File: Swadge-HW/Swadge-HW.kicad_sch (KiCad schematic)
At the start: 90 parts, among them J1 SAO, J2 PJ-307C, J3 PGM, P1 USB_C_Plug_USB2.0, Q1 Q_PMOS_GSD, SW1 YTS-D003-1A, SW2 YTS-D003-1A, SW3 YTS-D003-1A, SW4 YTS-D003-1A, SW5 YTS-D003-1A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

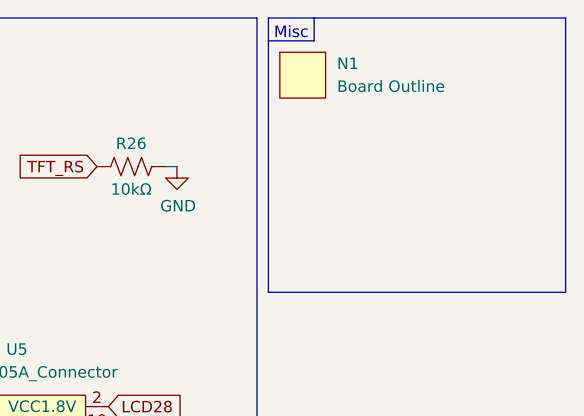
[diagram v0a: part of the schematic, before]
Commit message: Added condiment part
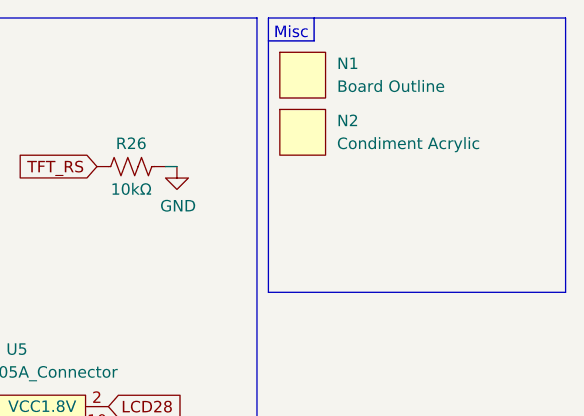
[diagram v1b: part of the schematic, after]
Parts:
- added N2: Condiment Acrylic, Swadge_Hotdog:condiment, symbol Swadge_Parts:NULL
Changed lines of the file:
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@@
+	)
+	(symbol
+		(lib_id "Swadge_Parts:NULL")
+		(at 313.69 25.4 0)
+		(unit 1)
+		(exclude_from_sim no)
+		(in_bom yes)
+		(on_board yes)
+		(dnp no)
+		(fields_autoplaced yes)
+		(property "Reference" "N2"
+			(at 317.5 24.1299 0)
+			(effects
+				(font
+					(size 1.27 1.27)
+				)
+				(justify left)
+			)
+		)
+		(property "Value" "Condiment Acrylic"
+			(at 317.5 26.6699 0)
+			(effects
+				(font
+					(size 1.27 1.27)
+				)
+				(justify left)
+			)
+		)
+		(property "Footprint" "Swadge_Hotdog:condiment"
+			(at 313.69 25.4 0)
+			(effects
+				(font
+					(size 1.27 1.27)
+				)
+				(hide yes)
+			)
+		)
+		(property "Datasheet" ""
+			(at 313.69 25.4 0)
+			(effects
+				(font
+					(size 1.27 1.27)
+				)
+				(hide yes)
+			)
+		)
+		(property "Description" ""
+			(at 313.69 25.4 0)
+			(effects
+				(font
+					(size 1.27 1.27)
+				)
+				(hide yes)
+			)
+		)
+		(instances
+			(project ""
+				(path "/770c762f-3a30-4864-b7da-de353459cdd6"
+					(reference "N2")
+					(unit 1)
+				)
+			)
+		)
 	)
 	(symbol

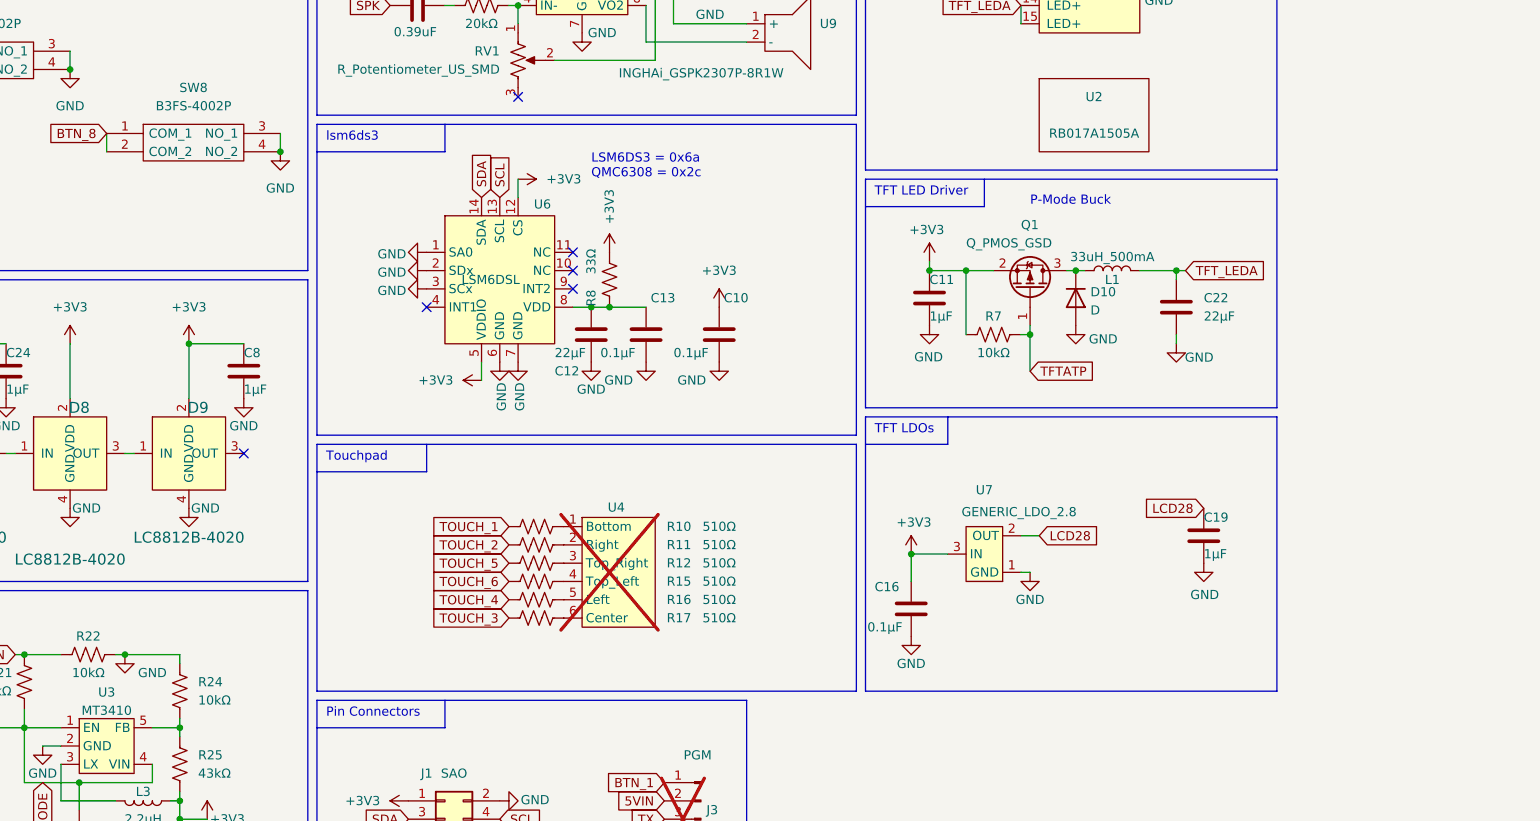
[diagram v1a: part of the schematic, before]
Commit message: Layout v0.5
Placement of 80% of SMD components
Add QMC6309
DNP D9
Move Power Switch to right dog
Bump Aux port over
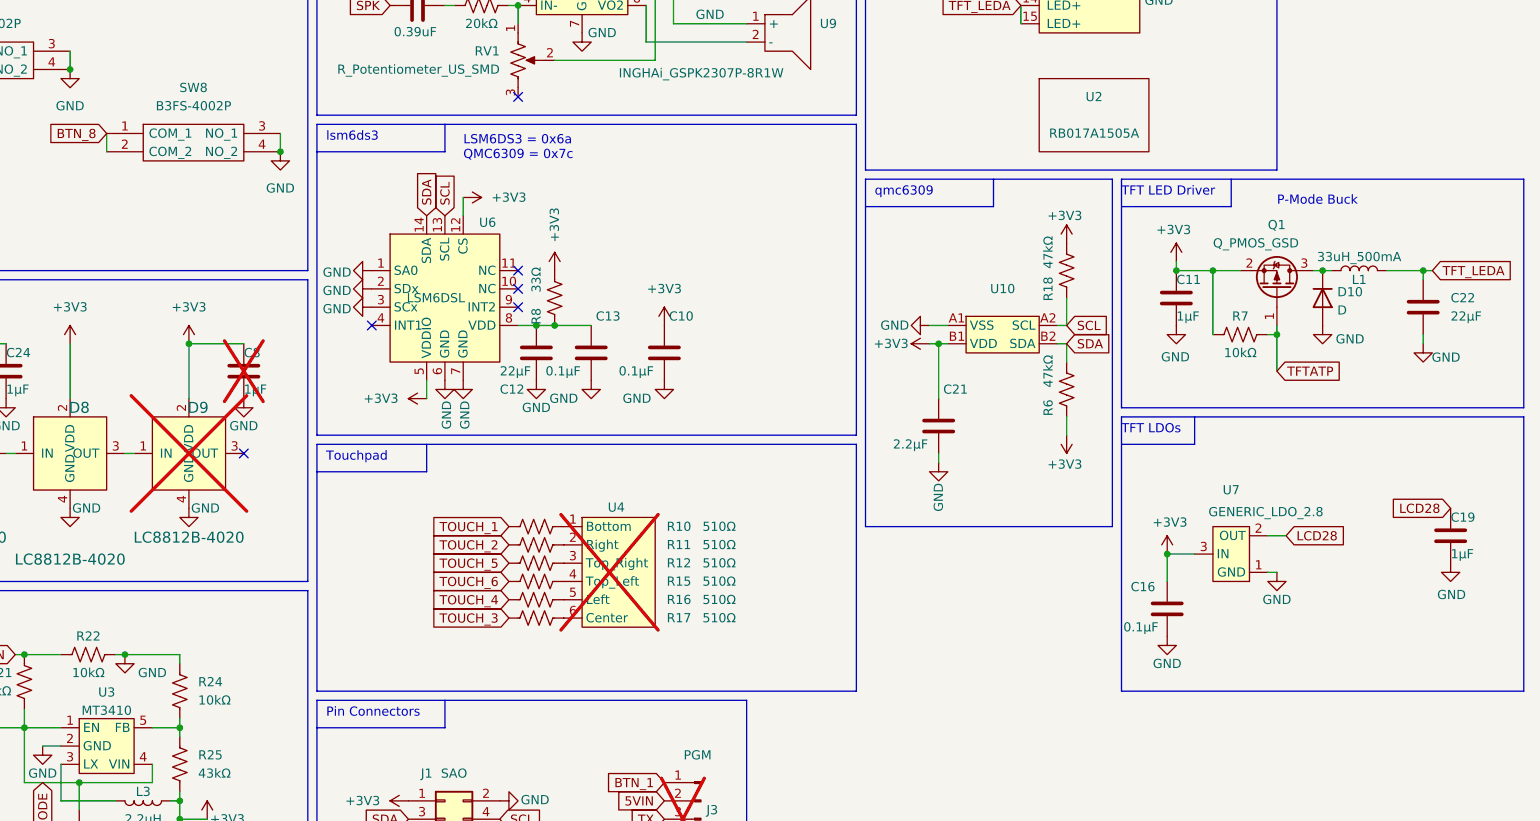
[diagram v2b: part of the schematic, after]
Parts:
- added C21: 2.2μF, Swadge_Parts:C_0603_1608Metric, symbol Swadge_Parts:C
- added R18, R6: 47kΩ, Swadge_Parts:R_0603_1608Metric, symbol Swadge_Parts:R_US
- added U10: ~, Swadge_Parts:BGA-4-.83x.83, symbol Swadge_Parts:QMC6309
- C8, D9: now not fitted
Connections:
- net +3V3: now also C21.1, R18.2, R6.1, U10.B1 (VDD)
- net GND: now also C21.2, U10.A1 (VSS)
- net SCL: now also R18.1, U10.A2 (SCL)
- net SDA: now also R6.2, U10.B2 (SDA)
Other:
- note added: "LSM6DS3 = 0x6a QMC6309 = 0x7c"
- note added: "qmc6309"
- note removed: "LSM6DS3 = 0x6a QMC6308 = 0x2c"
- moved on the sheet: C10, C11, C12, C13, C16, C19, C22, D10, L1, Q1, R7, R8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

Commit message: update from changes made by charlesl pre-order
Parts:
- N1: now not fitted
- N2: now not fitted; now left out of the parts list
- R18, R6: value 47kΩ -> 10kΩ; Cost @ 2.5k 0.0008 -> 0.0007; LCSC C23140 -> C25804
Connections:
- net +3V3: now also R18.1, R6.2; no longer R18.2, R6.1
- net SCL: now also R6.1; no longer R18.1
- net SDA: now also R18.2; no longer R6.2
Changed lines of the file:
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@@
 	)
 	(symbol
+		(lib_id "Swadge_Parts:R_US")
+		(at 279.4 113.03 180)
+		(unit 1)
+		(exclude_from_sim no)
+		(in_bom yes)
+		(on_board yes)
+		(dnp no)
+		(property "Reference" "R6"
+			(at 276.86 113.03 90)
+			(effects
+				(font
+					(size 1.27 1.27)
+				)
+			)
+		)
+		(property "Value" "10kΩ"
+			(at 281.94 113.03 90)
+			(effects
+				(font
+					(size 1.27 1.27)
+				)
+			)
+		)
+		(property "Footprint" "Swadge_Parts:R_0603_1608Metric"
+			(at 278.384 112.776 90)
+			(effects
+				(font
+					(size 1.27 1.27)
+				)
+				(hide yes)
+			)
+		)
+		(property "Datasheet" "~"
+			(at 276.86 113.03 90)
+			(effects
+				(font
+					(size 1.27 1.27)
+				)
+				(hide yes)
+			)
+		)
+		(property "Description" ""
+			(at 279.4 113.03 0)
+			(effects
+				(font
+					(size 1.27 1.27)
+				)
+				(hide yes)
+			)
+		)
+		(property "Digikey" "~"
+			(at 274.32 115.57 90)
+			(effects
+				(font
+					(size 1.27 1.27)
+				)
+				(hide yes)
+			)
+		)
+		(property "Cost100" "10"
+			(at 279.4 113.03 0)
+			(effects
+				(font
+					(size 0.254 0.254)
+				)
+				(hide yes)
+			)
+		)
+		(property "Substitutable" "Y"
+			(at 279.4 113.03 0)
+			(effects
+				(font
+					(size 0.254 0.254)
+				)
+				(hide yes)
+			)
+		)
+		(property "LCSC" "C25804"
+			(at 279.4 113.03 0)
+			(effects
+				(font
+					(size 1.27 1.27)
+				)
+				(hide yes)
+			)
+		)
+		(property "Cost @ 2.5k" "0.0007"
+			(at 279.4 113.03 0)
+			(effects
+				(font
+					(size 1.27 1.27)
+				)
+				(hide yes)
+			)
+		)
+		(pin "1"
+		)
+		(pin "2"
+		)
+		(instances
+			(project "Swadge-HW"
+				(path "/770c762f-3a30-4864-b7da-de353459cdd6"
+					(reference "R6")
+					(unit 1)
+				)
+			)
+		)
+	)
+	(symbol
 		(lib_id "Swadge_Parts:GND")
 		(at 332.74 153.67 0)
@@
 	)
 	(symbol
-		(lib_id "Swadge_Parts:R_US")
-		(at 279.4 113.03 180)
-		(unit 1)
-		(exclude_from_sim no)
-		(in_bom yes)
-		(on_board yes)
-		(dnp no)
-		(property "Reference" "R18"
-			(at 276.86 115.57 90)
-			(effects
-				(font
-					(size 1.27 1.27)
-				)
-			)
-		)
-		(property "Value" "47kΩ"
-			(at 276.86 110.49 90)
-			(effects
-				(font
-					(size 1.27 1.27)
-				)
-			)
-		)
-		(property "Footprint" "Swadge_Parts:R_0603_1608Metric"
-			(at 278.384 112.776 90)
-			(effects
-				(font
-					(size 1.27 1.27)
-				)
-				(hide yes)
-			)
-		)
-		(property "Datasheet" "~"
-			(at 279.4 113.03 0)
-			(effects
-				(font
-					(size 1.27 1.27)
-				)
-				(hide yes)
-			)
-		)
-		(property "Description" ""
-			(at 279.4 113.03 0)
-			(effects
-				(font
-					(size 1.27 1.27)
-				)
-				(hide yes)
-			)
-		)
-		(property "Cost100" "10"
-			(at 322.58 -12.7 0)
-			(effects
-				(font
-					(size 1.27 1.27)
-				)
-				(hide yes)
-			)
-		)
-		(property "Digikey" "~"
-			(at 322.58 -12.7 0)
-			(effects
-				(font
-					(size 1.27 1.27)
-				)
-				(hide yes)
-			)
-		)
-		(property "Substitutable" "Y"
-			(at 322.58 -12.7 0)
-			(effects
-				(font
-					(size 1.27 1.27)
-				)
-				(hide yes)
-			)
-		)
-		(property "LCSC" "C23140"
-			(at 279.4 113.03 0)
-			(effects
-				(font
-					(size 1.27 1.27)
-				)
-				(hide yes)
-			)
-		)
-		(property "Cost @ 2.5k" "0.0008"
-			(at 279.4 113.03 0)
-			(effects
-				(font
-					(size 1.27 1.27)
-				)
-				(hide yes)
-			)
-		)
-		(pin "1"
-		)
-		(pin "2"
-		)
-		(instances
-			(project "Swadge-HW"
-				(path "/770c762f-3a30-4864-b7da-de353459cdd6"
-					(reference "R18")
-					(unit 1)
-				)
-			)
-		)
-	)
-	(symbol
 		(lib_id "Swadge_Parts:YTS-D003-1A")
 		(at 129.54 63.5 0)
@@
 	)
 	(symbol
+		(lib_id "Swadge_Parts:R_US")
+		(at 279.4 129.54 180)
+		(unit 1)
+		(exclude_from_sim no)
+		(in_bom yes)
+		(on_board yes)
+		(dnp no)
+		(property "Reference" "R18"
+			(at 276.86 129.54 90)
+			(effects
+				(font
+					(size 1.27 1.27)
+				)
+			)
+		)
+		(property "Value" "10kΩ"
+			(at 281.94 129.54 90)
+			(effects
+				(font
+					(size 1.27 1.27)
+				)
+			)
+		)
+		(property "Footprint" "Swadge_Parts:R_0603_1608Metric"
+			(at 278.384 129.286 90)
+			(effects
+				(font
+					(size 1.27 1.27)
+				)
+				(hide yes)
+			)
+		)
+		(property "Datasheet" "~"
+			(at 276.86 129.54 90)
+			(effects
+				(font
+					(size 1.27 1.27)
+				)
+				(hide yes)
+			)
+		)
+		(property "Description" ""
+			(at 279.4 129.54 0)
+			(effects
+				(font
+					(size 1.27 1.27)
+				)
+				(hide yes)
+			)
+		)
+		(property "Digikey" "~"
+			(at 274.32 132.08 90)
+			(effects
+				(font
+					(size 1.27 1.27)
+				)
+				(hide yes)
+			)
+		)
+		(property "Cost100" "10"
+			(at 279.4 129.54 0)
+			(effects
+				(font
+					(size 0.254 0.254)
+				)
+				(hide yes)
+			)
+		)
+		(property "Substitutable" "Y"
+			(at 279.4 129.54 0)
+			(effects
+				(font
+					(size 0.254 0.254)
+				)
+				(hide yes)
+			)
+		)
+		(property "LCSC" "C25804"
+			(at 279.4 129.54 0)
+			(effects
+				(font
+					(size 1.27 1.27)
+				)
+				(hide yes)
+			)
+		)
+		(property "Cost @ 2.5k" "0.0007"
+			(at 279.4 129.54 0)
+			(effects
+				(font
+					(size 1.27 1.27)
+				)
+				(hide yes)
+			)
+		)
+		(pin "1"
+		)
+		(pin "2"
+		)
+		(instances
+			(project "Swadge-HW"
+				(path "/770c762f-3a30-4864-b7da-de353459cdd6"
+					(reference "R18")
+					(unit 1)
+				)
+			)
+		)
+	)
+	(symbol
 		(lib_id "Swadge_Parts:GND")
 		(at 294.64 120.65 0)
@@
 	)
 	(symbol
-		(lib_id "Swadge_Parts:R_US")
-		(at 279.4 129.54 180)
-		(unit 1)
-		(exclude_from_sim no)
-		(in_bom yes)
-		(on_board yes)
-		(dnp no)
-		(property "Reference" "R6"
-			(at 276.86 132.08 90)
-			(effects
-				(font
-					(size 1.27 1.27)
-				)
-			)
-		)
-		(property "Value" "47kΩ"
-			(at 276.86 127 90)
-			(effects
-				(font
-					(size 1.27 1.27)
-				)
-			)
-		)
-		(property "Footprint" "Swadge_Parts:R_0603_1608Metric"
-			(at 278.384 129.286 90)
-			(effects
-				(font
-					(size 1.27 1.27)
-				)
-				(hide yes)
-			)
-		)
-		(property "Datasheet" "~"
-			(at 279.4 129.54 0)
-			(effects
-				(font
-					(size 1.27 1.27)
-				)
-				(hide yes)
-			)
-		)
-		(property "Description" ""
-			(at 279.4 129.54 0)
-			(effects
-				(font
-					(size 1.27 1.27)
-				)
-				(hide yes)
-			)
-		)
-		(property "Cost100" "10"
-			(at 322.58 3.81 0)
-			(effects
-				(font
-					(size 1.27 1.27)
-				)
-				(hide yes)
-			)
-		)
-		(property "Digikey" "~"
-			(at 322.58 3.81 0)
-			(effects
-				(font
-					(size 1.27 1.27)
-				)
-				(hide yes)
-			)
-		)
-		(property "Substitutable" "Y"
-			(at 322.58 3.81 0)
-			(effects
-				(font
-					(size 1.27 1.27)
-				)
-				(hide yes)
-			)
-		)
-		(property "LCSC" "C23140"
-			(at 279.4 129.54 0)
-			(effects
-				(font
-					(size 1.27 1.27)
-				)
-				(hide yes)
-			)
-		)
-		(property "Cost @ 2.5k" "0.0008"
-			(at 279.4 129.54 0)
-			(effects
-				(font
-					(size 1.27 1.27)
-				)
-				(hide yes)
-			)
-		)
-		(pin "1"
-		)
-		(pin "2"
-		)
-		(instances
-			(project "Swadge-HW"
-				(path "/770c762f-3a30-4864-b7da-de353459cdd6"
-					(reference "R6")
-					(unit 1)
-				)
-			)
-		)
-	)
-	(symbol
 		(lib_id "Swadge_Parts:+3.3V")
 		(at 294.64 111.76 0)
@@
 		(unit 1)
 		(exclude_from_sim no)
-		(in_bom yes)
+		(in_bom no)
 		(on_board yes)
-		(dnp no)
+		(dnp yes)
 		(fields_autoplaced yes)
 		(property "Reference" "N2"
@@
 		(in_bom no)
 		(on_board yes)
-		(dnp no)
+		(dnp yes)
 		(fields_autoplaced yes)
 		(property "Reference" "N1"

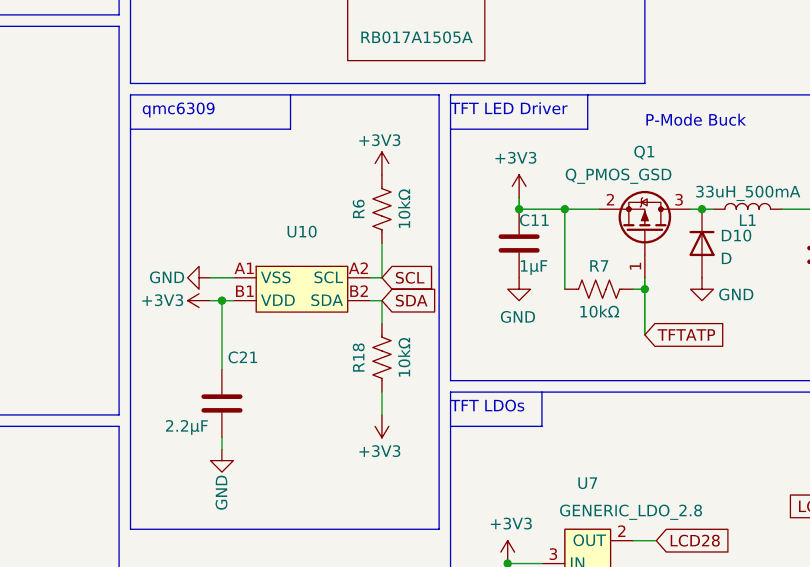
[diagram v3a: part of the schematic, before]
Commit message: Update to order for rev - before checking footprint on ESP32-S2
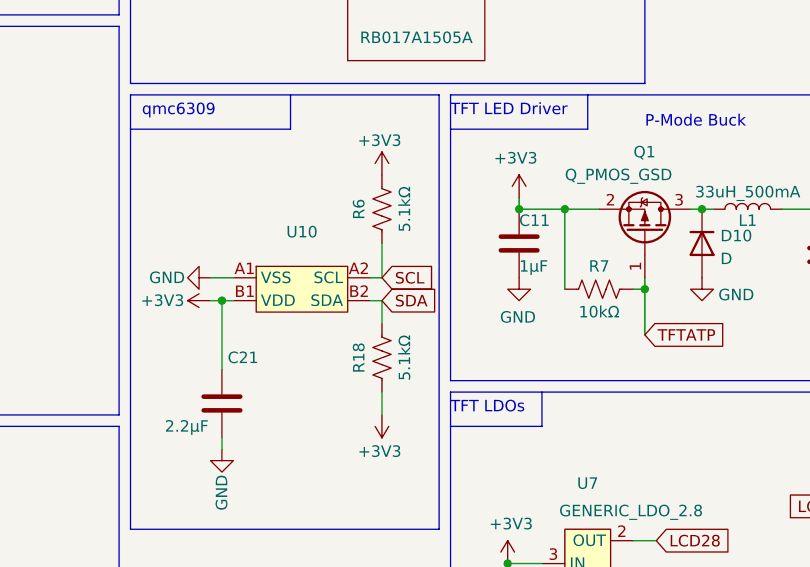
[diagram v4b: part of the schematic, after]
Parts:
- R18, R6: value 10kΩ -> 5.1kΩ; LCSC C25804 -> C23186
- RV1: LCSC C470765 -> C3020613
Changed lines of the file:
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@@
 			)
 		)
-		(property "Description" "RK10J11R001Y"
+		(property "Description" "RK10J11R0A0L"
 			(at 203.2 83.82 0)
 			(effects
@@
 			)
 		)
-		(property "LCSC" "C470765"
+		(property "LCSC" "C3020613"
 			(at 203.2 101.6 0)
 			(effects
@@
 			)
 		)
-		(property "Value" "10kΩ"
+		(property "Value" "5.1kΩ"
 			(at 281.94 113.03 90)
 			(effects
@@
 			)
 		)
-		(property "LCSC" "C25804"
+		(property "LCSC" "C23186"
 			(at 279.4 113.03 0)
 			(effects
@@
 			)
 		)
-		(property "Value" "10kΩ"
+		(property "Value" "5.1kΩ"
 			(at 281.94 129.54 90)
 			(effects
@@
 			)
 		)
-		(property "LCSC" "C25804"
+		(property "LCSC" "C23186"
 			(at 279.4 129.54 0)
 			(effects

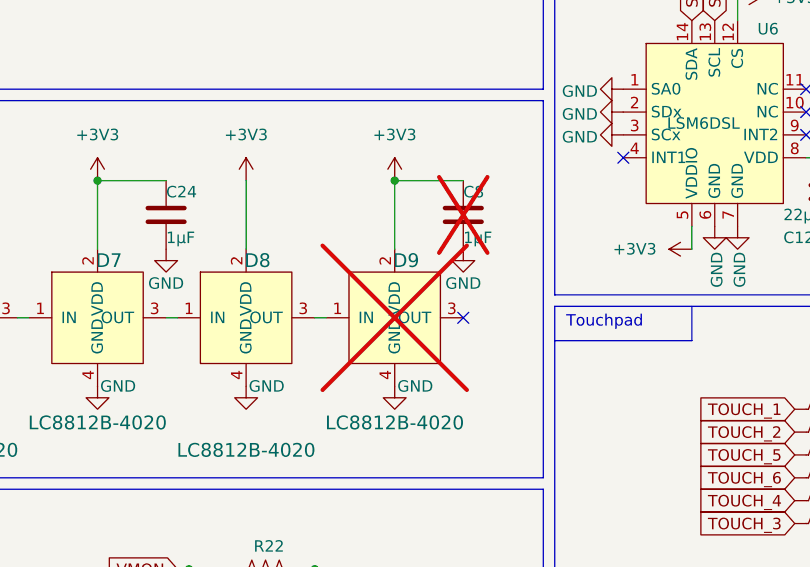
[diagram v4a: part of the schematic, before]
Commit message: Modify silk art and minor layout adjustments
Bump screen to right, bump switch inside, update silk art, nudge LED for clearance concerns
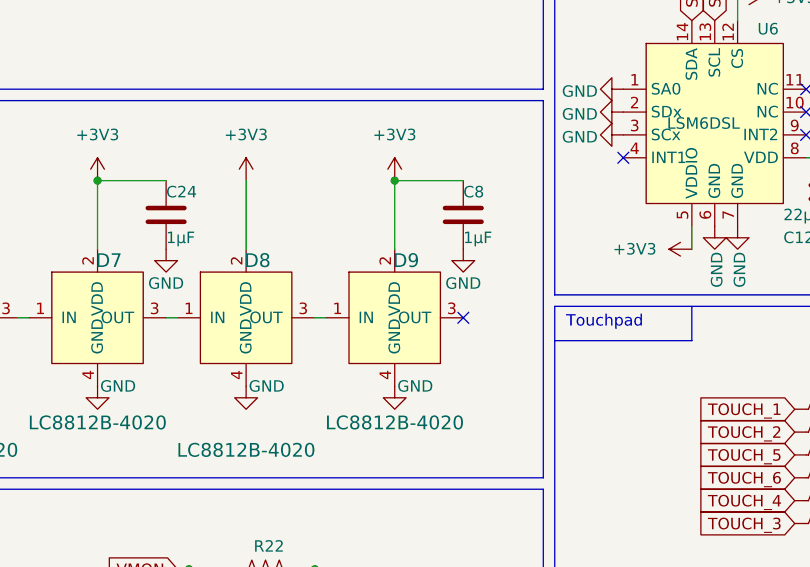
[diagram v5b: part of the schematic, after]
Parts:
- C8, D9: now fitted
- MK1: Notes (none) -> DNP
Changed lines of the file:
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@@
 		(in_bom yes)
 		(on_board no)
-		(dnp yes)
+		(dnp no)
 		(property "Reference" "D9"
 			(at 158.75 132.08 0)
@@
 		(in_bom yes)
 		(on_board no)
-		(dnp yes)
+		(dnp no)
 		(property "Reference" "C8"
 			(at 165.1 124.46 0)
@@
 			(effects
 				(font
+					(size 1.27 1.27)
+				)
+				(hide yes)
+			)
+		)
+		(property "Notes" "DNP"
+			(at 419.1 68.58 0)
+			(effects
+				(font
